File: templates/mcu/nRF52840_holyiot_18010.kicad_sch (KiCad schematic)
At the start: 3 parts, among them J1 SWD, U1 nRF52840_holyiot_18010

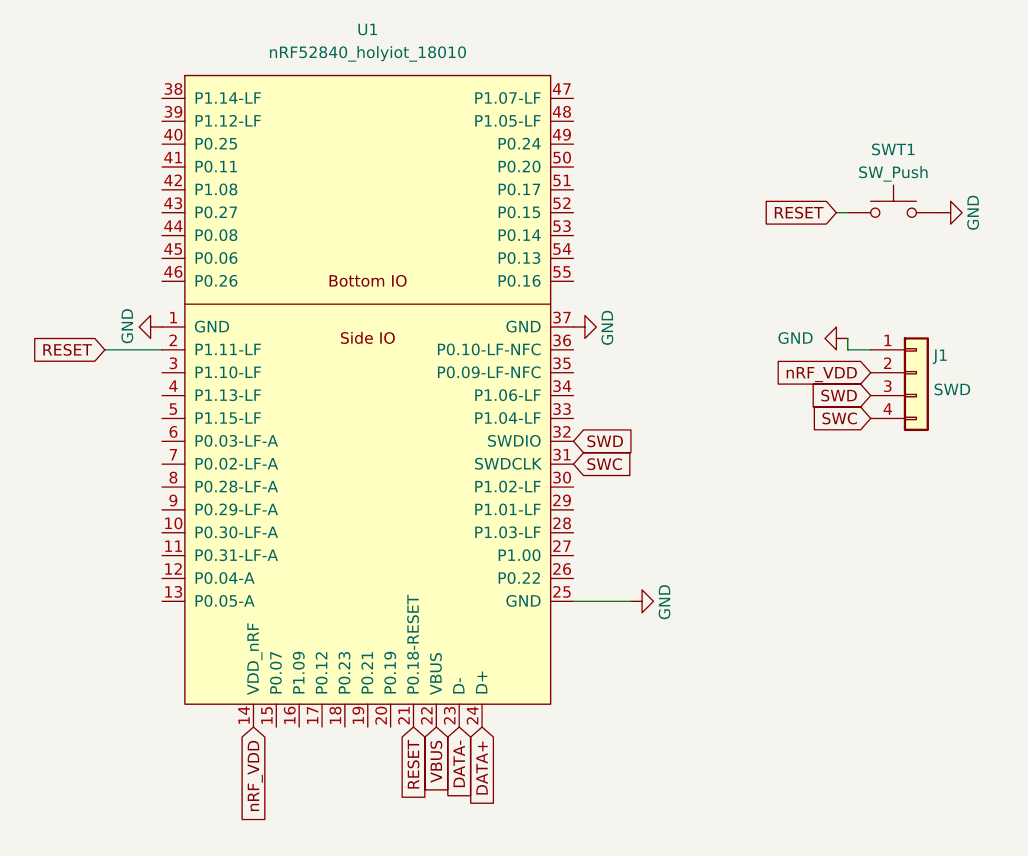
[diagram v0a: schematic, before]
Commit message: update mcu nRF52840_holyiot_18010 annotation
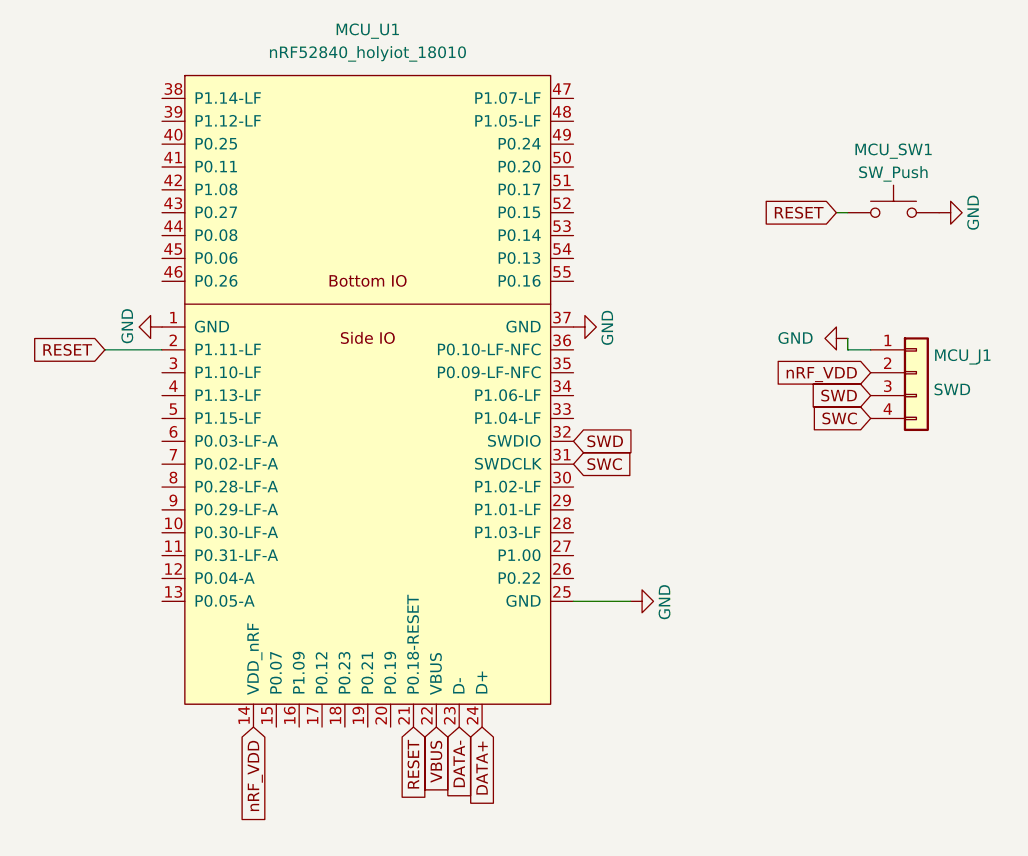
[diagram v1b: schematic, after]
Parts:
- renumbered J1 to MCU_J1, SWT1 to MCU_SW1, U1 to MCU_U1
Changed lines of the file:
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@@
 		(dnp no)
 		(fields_autoplaced yes)
-		(property "Reference" "U1"
+		(property "Reference" "MCU_U1"
 			(at 76.2 22.86 0)
 			(effects
@@
 		)
 		(instances
-			(project "ergo_cai"
-				(path "/4ad52d44-7e09-4b14-9ca9-1745a5702ae6/1defd50b-9fa9-4121-9475-90ecc1018df4"
-					(reference "U1")
+			(project ""
+				(path "/a09f68bc-a7d5-404f-ac28-eebdcd98bea9"
+					(reference "MCU_U1")
+					(unit 1)
+				)
+			)
+			(project "nRF52840_holyiot_18010"
+				(path "/a09f68bc-a7d5-404f-ac28-eebdcd98bea9"
+					(reference "MCU_U1")
 					(unit 1)
 				)
@@
 				)
 			)
+			(project "nRF52840_holyiot_18010"
+				(path "/a09f68bc-a7d5-404f-ac28-eebdcd98bea9"
+					(reference "#PWR?")
+					(unit 1)
+				)
+			)
 		)
 	)
@@
 		(on_board yes)
 		(dnp no)
-		(property "Reference" "J1"
+		(property "Reference" "MCU_J1"
 			(at 139.065 59.055 0)
 			(effects
@@
 		)
 		(instances
-			(project "ergo_cai"
-				(path "/4ad52d44-7e09-4b14-9ca9-1745a5702ae6/1defd50b-9fa9-4121-9475-90ecc1018df4"
-					(reference "J1")
+			(project ""
+				(path "/a09f68bc-a7d5-404f-ac28-eebdcd98bea9"
+					(reference "MCU_J1")
+					(unit 1)
+				)
+			)
+			(project "nRF52840_holyiot_18010"
+				(path "/a09f68bc-a7d5-404f-ac28-eebdcd98bea9"
+					(reference "MCU_J1")
 					(unit 1)
 				)
@@
 				)
 			)
+			(project "nRF52840_holyiot_18010"
+				(path "/a09f68bc-a7d5-404f-ac28-eebdcd98bea9"
+					(reference "#PWR?")
+					(unit 1)
+				)
+			)
 		)
 	)
@@
 				)
 			)
+			(project "nRF52840_holyiot_18010"
+				(path "/a09f68bc-a7d5-404f-ac28-eebdcd98bea9"
+					(reference "#PWR?")
+					(unit 1)
+				)
+			)
 		)
 	)
@@
 				)
 			)
+			(project "nRF52840_holyiot_18010"
+				(path "/a09f68bc-a7d5-404f-ac28-eebdcd98bea9"
+					(reference "#PWR?")
+					(unit 1)
+				)
+			)
 		)
 	)
@@
 		(on_board yes)
 		(dnp no)
-		(property "Reference" "SWT1"
+		(property "Reference" "MCU_SW1"
 			(at 134.62 36.195 0)
 			(effects
@@
 		)
 		(instances
-			(project "ergo_cai"
-				(path "/4ad52d44-7e09-4b14-9ca9-1745a5702ae6/1defd50b-9fa9-4121-9475-90ecc1018df4"
-					(reference "SWT1")
+			(project ""
+				(path "/a09f68bc-a7d5-404f-ac28-eebdcd98bea9"
+					(reference "MCU_SW1")
+					(unit 1)
+				)
+			)
+			(project "nRF52840_holyiot_18010"
+				(path "/a09f68bc-a7d5-404f-ac28-eebdcd98bea9"
+					(reference "MCU_SW1")
 					(unit 1)
 				)
@@
 				)
 			)
-		)
-	)
+			(project "nRF52840_holyiot_18010"
+				(path "/a09f68bc-a7d5-404f-ac28-eebdcd98bea9"
+					(reference "#PWR?")
+					(unit 1)
+				)
+			)
+		)
+	)
+	(sheet_instances
+		(path "/"
+			(page "1")
+		)
+	)

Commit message: update footprint lib to ergocai.pretty
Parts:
- MCU_J1: footprint ErgoCai:Connector_THT_1x4_2.54 -> ErgoCai.pretty:Connector_THT_1x4_2.54
- MCU_U1: footprint ErgoCai:nRF52840_holyiot_18010 -> ErgoCai.pretty:nRF52840_holyiot_18010
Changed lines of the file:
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@@
 			)
 		)
-		(property "Footprint" "ErgoCai:nRF52840_holyiot_18010"
+		(property "Footprint" "ErgoCai.pretty:nRF52840_holyiot_18010"
 			(at 76.2 17.78 0)
 			(effects
@@
 		(instances
 			(project ""
-				(path "/a09f68bc-a7d5-404f-ac28-eebdcd98bea9"
+				(path "/4ad52d44-7e09-4b14-9ca9-1745a5702ae6/6ca11bcf-11a9-4f93-970b-96b1b3348f3d"
 					(reference "MCU_U1")
 					(unit 1)
@@
 		)
 		(instances
-			(project "ergo_cai"
-				(path "/4ad52d44-7e09-4b14-9ca9-1745a5702ae6/1defd50b-9fa9-4121-9475-90ecc1018df4"
+			(project ""
+				(path "/4ad52d44-7e09-4b14-9ca9-1745a5702ae6/6ca11bcf-11a9-4f93-970b-96b1b3348f3d"
 					(reference "#PWR013")
 					(unit 1)
@@
 			)
 		)
-		(property "Footprint" "ErgoCai:Connector_THT_1x4_2.54"
+		(property "Footprint" "ErgoCai.pretty:Connector_THT_1x4_2.54"
 			(at 137.16 60.96 0)
 			(effects
@@
 		(instances
 			(project ""
-				(path "/a09f68bc-a7d5-404f-ac28-eebdcd98bea9"
+				(path "/4ad52d44-7e09-4b14-9ca9-1745a5702ae6/6ca11bcf-11a9-4f93-970b-96b1b3348f3d"
 					(reference "MCU_J1")
 					(unit 1)
@@
 		)
 		(instances
-			(project "ergo_cai"
-				(path "/4ad52d44-7e09-4b14-9ca9-1745a5702ae6/1defd50b-9fa9-4121-9475-90ecc1018df4"
+			(project ""
+				(path "/4ad52d44-7e09-4b14-9ca9-1745a5702ae6/6ca11bcf-11a9-4f93-970b-96b1b3348f3d"
 					(reference "#PWR09")
 					(unit 1)
@@
 		)
 		(instances
-			(project "ergo_cai"
-				(path "/4ad52d44-7e09-4b14-9ca9-1745a5702ae6/1defd50b-9fa9-4121-9475-90ecc1018df4"
+			(project ""
+				(path "/4ad52d44-7e09-4b14-9ca9-1745a5702ae6/6ca11bcf-11a9-4f93-970b-96b1b3348f3d"
 					(reference "#PWR08")
 					(unit 1)
@@
 		)
 		(instances
-			(project "ergo_cai"
-				(path "/4ad52d44-7e09-4b14-9ca9-1745a5702ae6/1defd50b-9fa9-4121-9475-90ecc1018df4"
+			(project ""
+				(path "/4ad52d44-7e09-4b14-9ca9-1745a5702ae6/6ca11bcf-11a9-4f93-970b-96b1b3348f3d"
 					(reference "#PWR011")
 					(unit 1)
@@
 		)
 		(instances
-			(project ""
-				(path "/a09f68bc-a7d5-404f-ac28-eebdcd98bea9"
-					(reference "MCU_SW1")
-					(unit 1)
-				)
-			)
 			(project "nRF52840_holyiot_18010"
 				(path "/a09f68bc-a7d5-404f-ac28-eebdcd98bea9"
@@
 		)
 		(instances
-			(project "ergo_cai"
-				(path "/4ad52d44-7e09-4b14-9ca9-1745a5702ae6/1defd50b-9fa9-4121-9475-90ecc1018df4"
+			(project ""
+				(path "/4ad52d44-7e09-4b14-9ca9-1745a5702ae6/6ca11bcf-11a9-4f93-970b-96b1b3348f3d"
 					(reference "#PWR010")
 					(unit 1)

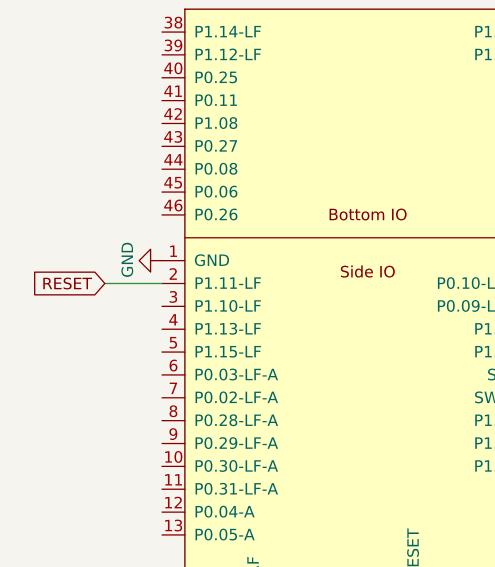
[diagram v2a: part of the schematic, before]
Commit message: remove useless reset in nrf52840
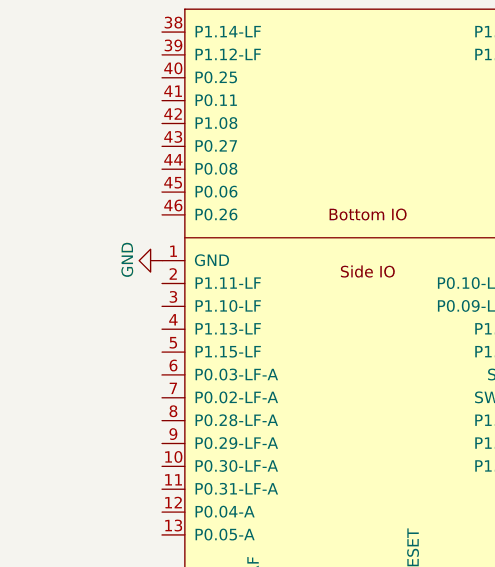
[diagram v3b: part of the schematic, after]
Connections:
- net RESET: no longer MCU_U1.2 (P1.11-LF)
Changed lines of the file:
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@@
-	(wire
-		(pts
-			(xy 46.99 58.42) (xy 53.34 58.42)
-		)
-		(stroke
-			(width 0)
-			(type default)
-		)
-	)
 	(wire
 		(pts
@@
 			(effects
 				(font
-					(size 1.27 1.27)
-				)
-				(justify right)
-				(hide yes)
-			)
-		)
-	)
-	(global_label "RESET"
-		(shape input)
-		(at 46.99 58.42 180)
-		(fields_autoplaced yes)
-		(effects
-			(font
-				(size 1.27 1.27)
-			)
-			(justify right)
-		)
-		(property "Intersheetrefs" "${INTERSHEET_REFS}"
-			(at 38.2597 58.42 0)
-			(effects
-				(font
